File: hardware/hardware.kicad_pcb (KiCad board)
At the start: 2 copper layers, 116.8 x 67.3 mm, 20 parts, among them J1 Conn_01x04_Male, J2 DIN-5_180degree, J3 DIN-5_180degree, SW1 SW_Push, U1 Teensy3.2, U2 TeensyAudioShield3.2, U3 6N139

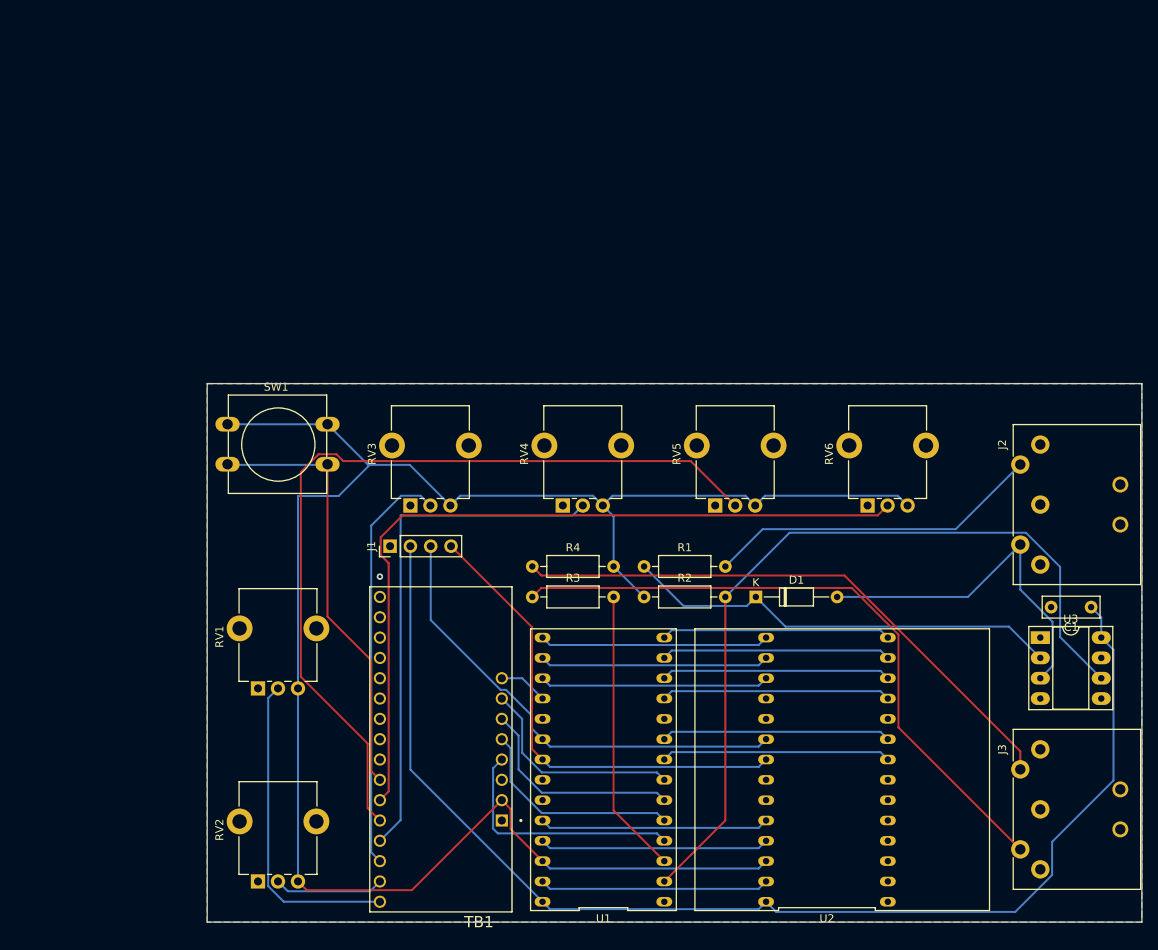
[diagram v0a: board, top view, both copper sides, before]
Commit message: Add extra controls, convert pcb to use connectors
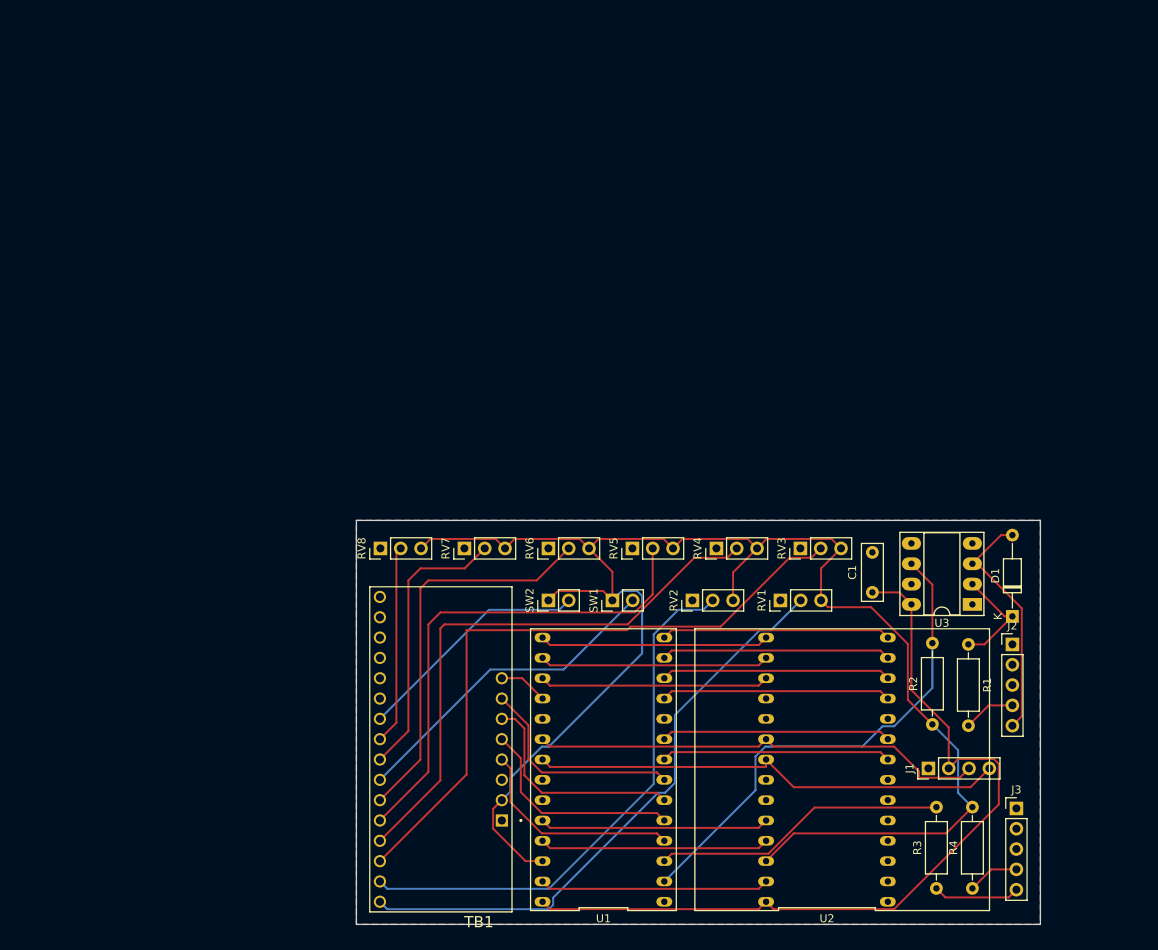
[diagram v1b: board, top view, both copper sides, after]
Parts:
- added RV7: R_POT, Connector_PinHeader_2.54mm:PinHeader_1x03_P2.54mm_Vertical, F.Cu at (102.0, 109.5)
- added RV8: R_POT, Connector_PinHeader_2.54mm:PinHeader_1x03_P2.54mm_Vertical, F.Cu at (91.5, 109.5)
- added SW2: SW_Push, Connector_PinHeader_2.54mm:PinHeader_1x02_P2.54mm_Vertical, F.Cu at (112.5, 116.0)
- J2, J3: footprint hardware:SDS-50J -> Connector_PinHeader_2.54mm:PinHeader_1x05_P2.54mm_Vertical
- RV1, RV2, RV3, RV4, RV5, RV6: footprint Potentiometer_THT:Potentiometer_Alpha_RD901F-40-00D_Single_Vertical_CircularHoles -> Connector_PinHeader_2.54mm:PinHeader_1x03_P2.54mm_Vertical
- SW1: footprint Button_Switch_THT:SW_PUSH-12mm -> Connector_PinHeader_2.54mm:PinHeader_1x02_P2.54mm_Vertical
- moved J1 72.8 mm to (160.0, 137.0)
- moved R4 68.2 mm to (165.5, 152.0), turned to 90 degrees
- moved RV1 66.2 mm to (141.5, 116.0)
- moved RV2 64.7 mm to (130.5, 116.0)
- moved R3 62.3 mm to (161.0, 152.0), turned to 90 degrees
- moved SW1 52.9 mm to (120.5, 116.0), turned to 90 degrees
- moved RV3 49.0 mm to (144.0, 109.5)
- moved R1 41.7 mm to (165.0, 121.5), turned to 270 degrees
- moved RV6 40.3 mm to (112.5, 109.5)
- moved R2 39.4 mm to (160.5, 131.5), turned to 90 degrees
- moved D1 32.2 mm to (170.5, 118.0), turned to 90 degrees
- moved C1 27.4 mm to (153.0, 115.0), turned to 90 degrees
- moved J2 25.2 mm to (170.5, 121.5), turned to 0 degrees
- moved RV4 19.9 mm to (133.5, 109.5)
- moved RV5 11.7 mm to (123.0, 109.5)
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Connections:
- J2 pad 1: Net-(J2-Pad1) -> (no net)
- J2 pad 2: Net-(J2-Pad2) -> (no net)
- J2 pad 3: Net-(J2-Pad3) -> (no net)
- J3 pad 1: Net-(J3-Pad1) -> (no net)
- J3 pad 3: Net-(J3-Pad3) -> (no net)
- TB1 pad 16: Net-(TB1-Pad16) -> /LFO1_Amp
- TB1 pad 17: Net-(TB1-Pad17) -> /LFO1_Freq
- TB1 pad 18: Net-(TB1-Pad18) -> /LFO1_WAV
- TB1 pad 19: Net-(TB1-Pad19) -> (no net)
- TB1 pad 20: Net-(TB1-Pad20) -> (no net)
- TB1 pad 21: Net-(TB1-Pad21) -> (no net)
- TB1 pad 22: Net-(TB1-Pad22) -> (no net)
- TB1 pad 23: Net-(TB1-Pad23) -> (no net)
- TB1 pad 24: Net-(TB1-Pad24) -> (no net)
- U1 pad 10: /D8 -> (no net)
- U1 pad 19: /A3 -> (no net)
- U1 pad 22: /A6 -> (no net)
- U1 pad 23: /A7 -> (no net)
- U2 pad 10: Net-(U2-Pad10) -> (no net)
- U2 pad 18: Net-(U2-Pad18) -> (no net)
- U2 pad 19: Net-(U2-Pad19) -> (no net)
- U2 pad 2: Net-(U2-Pad2) -> (no net)
- U2 pad 22: Net-(U2-Pad22) -> (no net)
- U2 pad 23: Net-(U2-Pad23) -> (no net)
- U2 pad 3: Net-(U2-Pad3) -> (no net)
- U2 pad 4: Net-(U2-Pad4) -> (no net)
- U2 pad 5: Net-(U2-Pad5) -> (no net)
- U2 pad 6: Net-(U2-Pad6) -> (no net)
- U2 pad 7: Net-(U2-Pad7) -> (no net)
- U3 pad 1: Net-(U3-Pad1) -> (no net)
- U3 pad 4: Net-(U3-Pad4) -> (no net)
- U3 pad 7: Net-(U3-Pad7) -> (no net)
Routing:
- net Net-(J3-Pad5): track 81.8 -> 10.9 mm
- net Net-(J3-Pad4): track 72.8 -> 6.49 mm
- net /Filter_Res: track 13.8 -> 67.9 mm
- net +5V: track 156.0 -> 103.6 mm
- net /ADSR_Release: track 98.7 -> 49.2 mm
- net /ADSR_Sustain: track 105.5 -> 62.4 mm
- net Net-(D1-Pad1): track 55.2 -> 13.6 mm
- net /MIDI_IN: track 101.7 -> 62.6 mm
- net Net-(J2-Pad4): track 42.1 -> 6.55 mm
- net /LFO1_Amp: track 0.00 -> 35.1 mm
- net /Filter_Freq: track 40.0 -> 74.5 mm
- net /ADSR_Attack: track 51.8 -> 81.9 mm
- net /LFO1_WAV: track 0.00 -> 29.7 mm
- net +3V3: track 233.6 -> 204.4 mm
- net /LFO1_Freq: track 0.00 -> 24.9 mm
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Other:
- board size 116.8 x 67.3 mm -> 85.5 x 50.5 mm

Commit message: Add pull-downs to pcb
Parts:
- added R5: 10k, Resistor_THT:R_Axial_DIN0207_L6.3mm_D2.5mm_P10.16mm_Horizontal, F.Cu at (105.5, 147.0)
- added R6: 10k, Resistor_THT:R_Axial_DIN0207_L6.3mm_D2.5mm_P10.16mm_Horizontal, F.Cu at (105.5, 150.0)
- U3: value 6N139 -> 6N138
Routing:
- net /LFO1_WAV: track 29.7 -> 63.3 mm
- net /OSC1_WAV: track 40.9 -> 57.4 mm

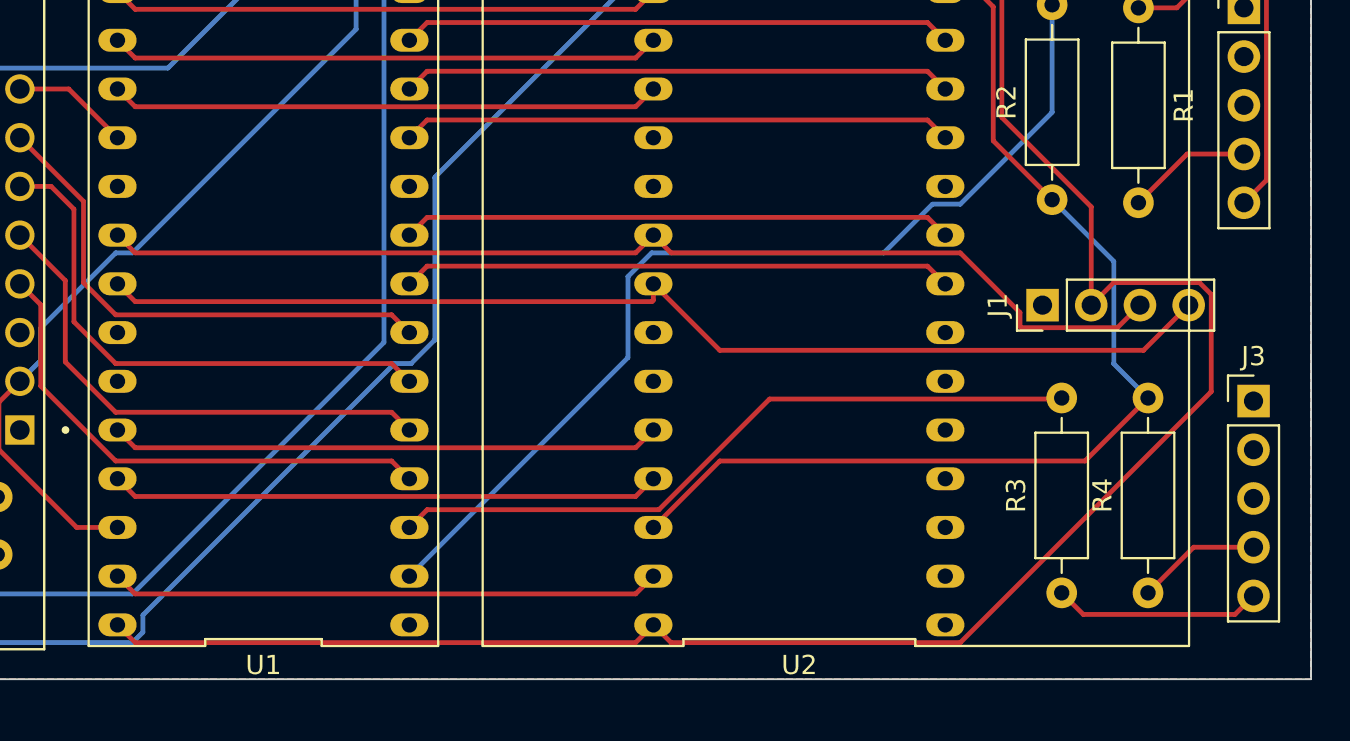
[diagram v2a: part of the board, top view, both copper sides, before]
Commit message: Remove MIDI out and add RGB LED header
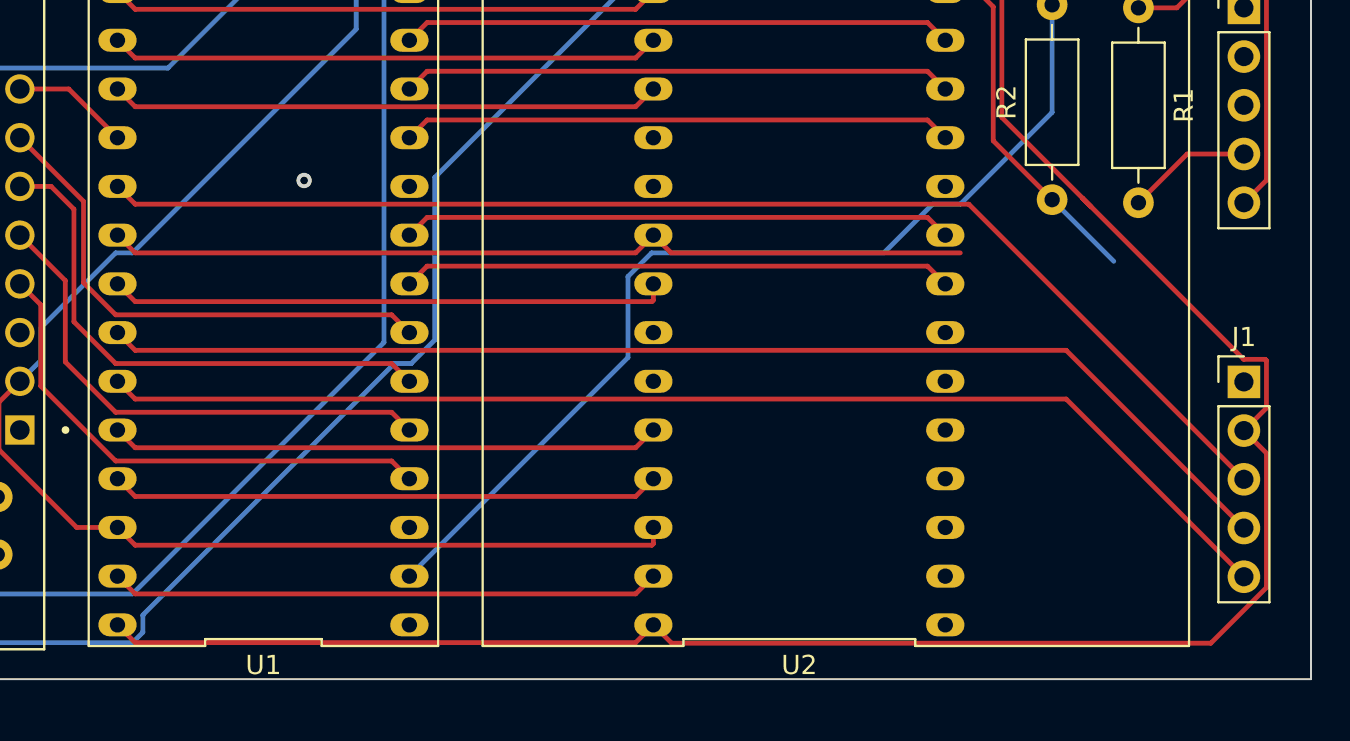
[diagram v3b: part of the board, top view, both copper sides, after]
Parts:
- removed J3: DIN-5_180degree, Connector_PinHeader_2.54mm:PinHeader_1x05_P2.54mm_Vertical
- removed R3, R4: 47, Resistor_THT:R_Axial_DIN0207_L6.3mm_D2.5mm_P10.16mm_Horizontal
- J1: value Conn_01x04_Male -> Conn_01x05_Male; footprint Connector_PinHeader_2.54mm:PinHeader_1x04_P2.54mm_Vertical -> Connector_PinHeader_2.54mm:PinHeader_1x05_P2.54mm_Vertical
- moved J1 11.2 mm to (170.5, 141.0), turned to 0 degrees
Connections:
- net /A2 renamed /MULT_SIG
- net /D2 renamed /MULT_S0
- net /D3 renamed /MULT_S1
- net /D4 renamed /MULT_S2
- net /D5 renamed /MULT_S3
- J1 pad 3: /SDA -> /RGB_R
- J1 pad 4: /SCL -> /RGB_G
- U1 pad 19: (no net) -> /RGB_R
- U1 pad 22: (no net) -> /RGB_G
- U1 pad 23: (no net) -> /RGB_B
- U1 pad 3: /MIDI_OUT -> (no net)
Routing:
- net /RGB_R: track 0.00 -> 65.1 mm
- net /RGB_G: track 0.00 -> 63.0 mm
- net /RGB_B: track 0.00 -> 63.0 mm
- net /MIDI_OUT: track 36.8 -> 0.00 mm
- net /SCL: track 59.5 -> 29.2 mm
- net /SDA: track 57.0 -> 45.1 mm
- net Net-(J3-Pad5): track 10.9 -> 0.00 mm
- net +5V: track 103.6 -> 111.0 mm
- net +3V3: track 204.4 -> 197.2 mm
- net Net-(J3-Pad4): track 6.49 -> 0.00 mm
- net GND: vias 0 -> 1

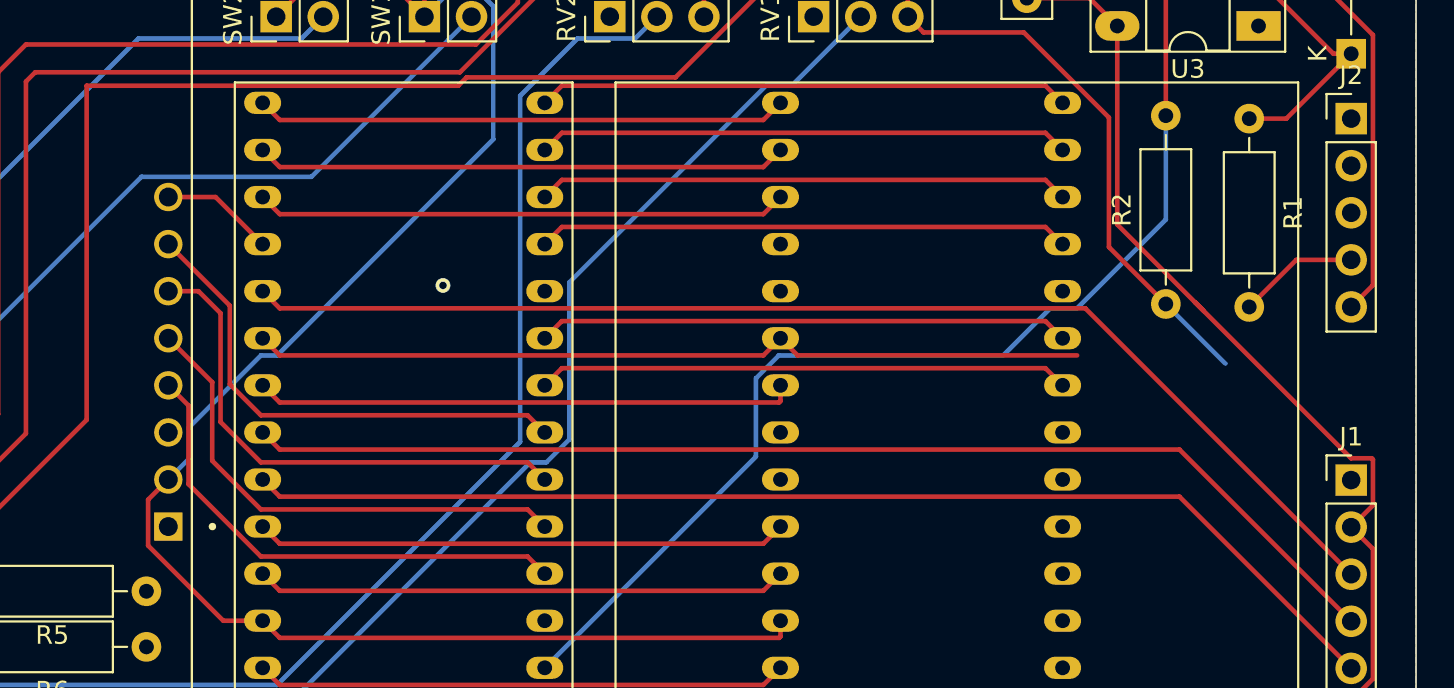
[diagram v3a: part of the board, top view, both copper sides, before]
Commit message: Move RGB_R and MULT address pins to get RGB on PWM pin
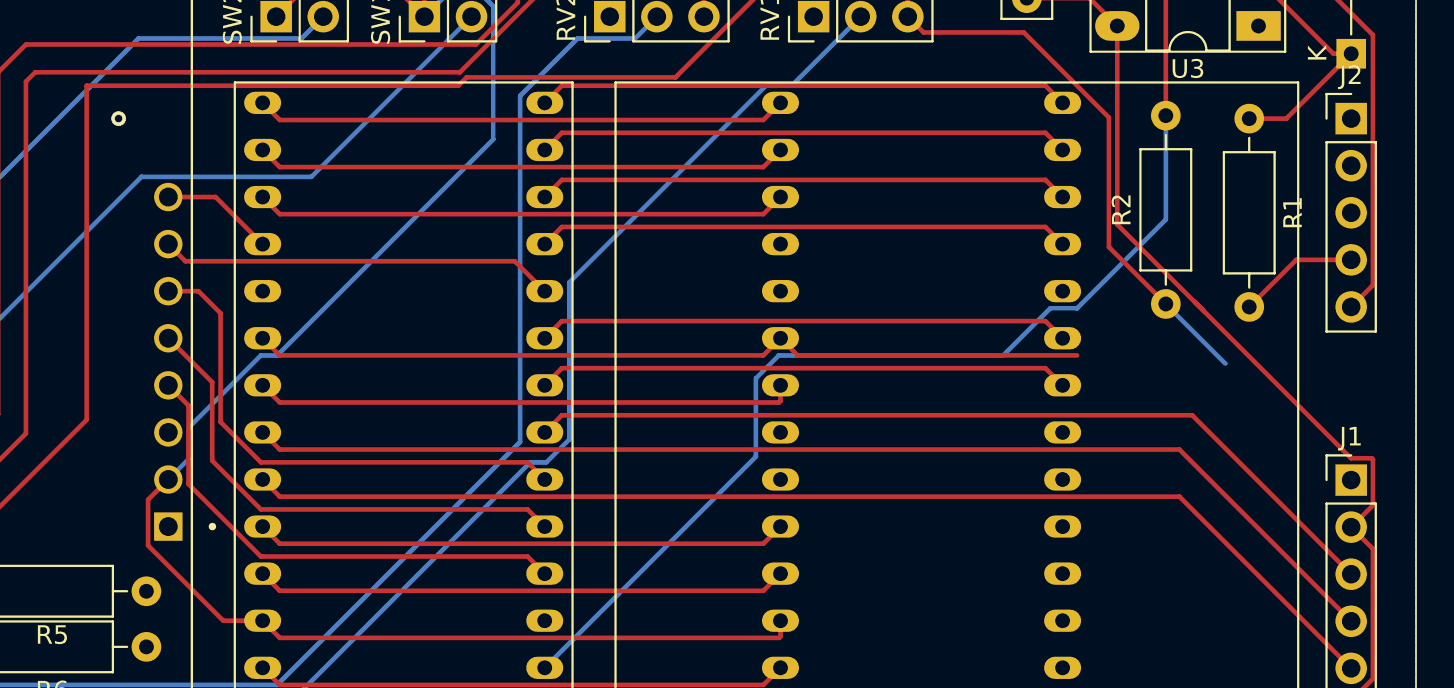
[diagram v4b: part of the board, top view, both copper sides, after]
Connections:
- U1 pad 10: (no net) -> /MULT_S3
- U1 pad 19: /RGB_R -> (no net)
- U1 pad 7: /MULT_S3 -> /RGB_R
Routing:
- net /RGB_R: track 65.1 -> 47.4 mm
- net /MULT_S3: track 27.0 -> 21.4 mm
